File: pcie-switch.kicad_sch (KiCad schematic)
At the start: 139 parts, among them J5 Tag-Connect_TC2050-IDC-NL_2x5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, Q1 BSS138PW,115, Q2 BSS138PW,115, Q3 BSS138PW,115, Q4 BSS138PW,115, Q5 BSS138PW,115, U4 PI7C9X3G606GP, U5 NTS0302JKZ, U6 93AA66C_SOIC

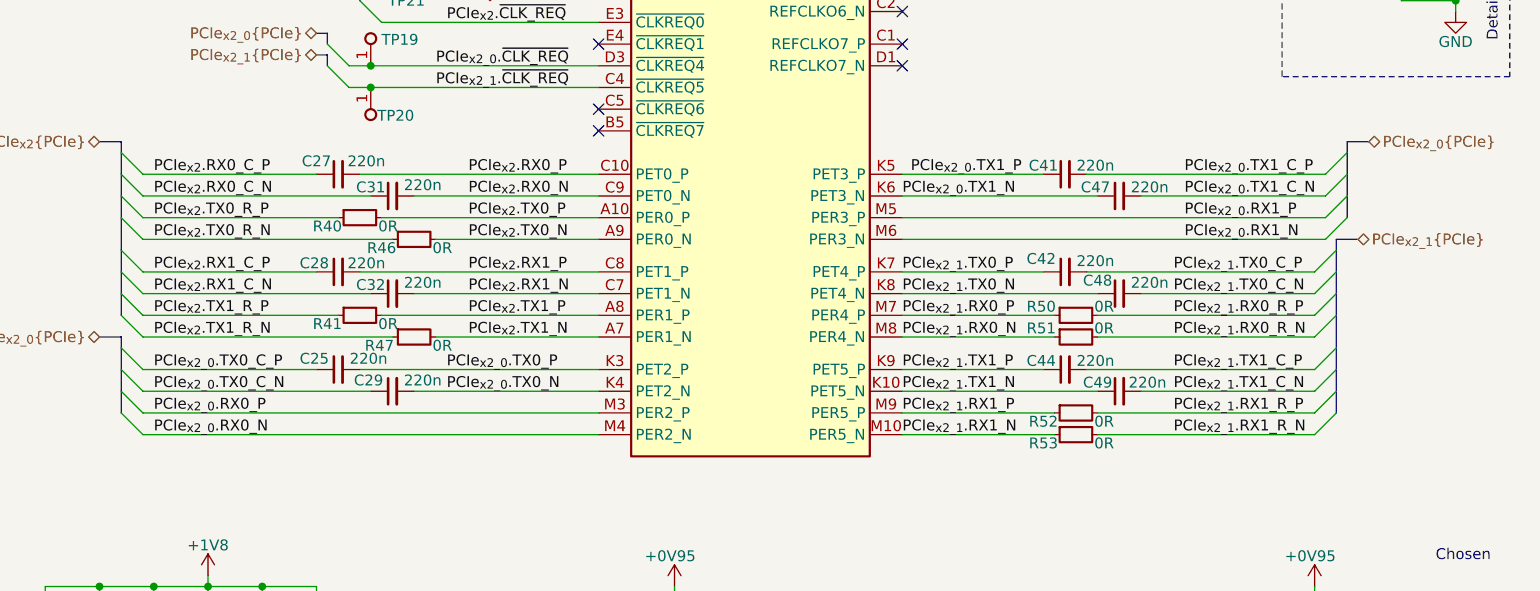
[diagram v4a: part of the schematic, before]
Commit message: [#101859] Add HS fanout from connectors
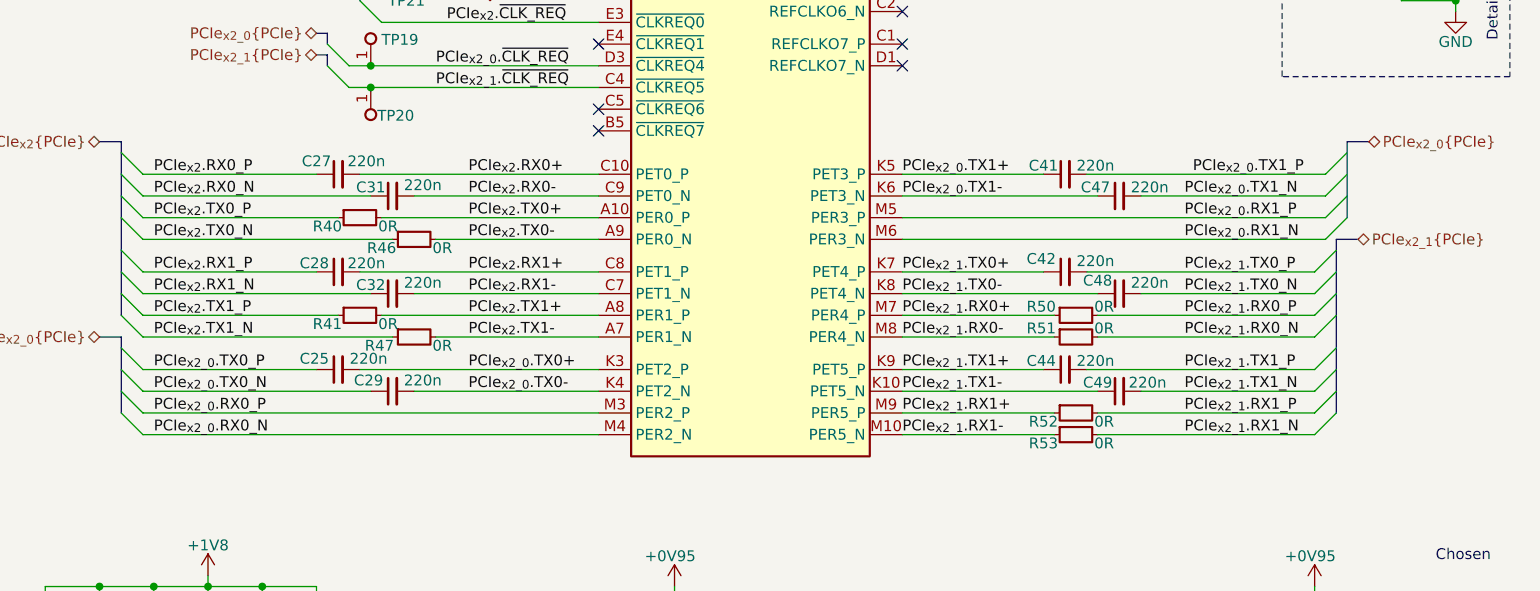
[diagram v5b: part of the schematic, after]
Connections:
- net PCIe_{x2_0}.TX0_C_N is gone; now on net PCIe_{x2_0}.TX0_N: C29.1
- net PCIe_{x2_0}.TX0_C_P is gone; now on net PCIe_{x2_0}.TX0_P: C25.1
- net PCIe_{x2_0}.TX1_C_N is gone; now on net PCIe_{x2_0}.TX1_N: C47.2
- net PCIe_{x2_0}.TX1_C_P is gone; now on net PCIe_{x2_0}.TX1_P: C41.2
- net PCIe_{x2_1}.RX0_R_N is gone; now on net PCIe_{x2_1}.RX0_N: R51.2
- net PCIe_{x2_1}.RX0_R_P is gone; now on net PCIe_{x2_1}.RX0_P: R50.2
- net PCIe_{x2_1}.RX1_R_N is gone; now on net PCIe_{x2_1}.RX1_N: R53.2
- net PCIe_{x2_1}.RX1_R_P is gone; now on net PCIe_{x2_1}.RX1_P: R52.2
- net PCIe_{x2_1}.TX0_C_N is gone; now on net PCIe_{x2_1}.TX0_N: C48.2
- net PCIe_{x2_1}.TX0_C_P is gone; now on net PCIe_{x2_1}.TX0_P: C42.2
- net PCIe_{x2_1}.TX1_C_N is gone; now on net PCIe_{x2_1}.TX1_N: C49.2
- net PCIe_{x2_1}.TX1_C_P is gone; now on net PCIe_{x2_1}.TX1_P: C44.2
- net PCIe_{x2}.RX0_C_N is gone; now on net PCIe_{x2}.RX0_N: C31.1
- net PCIe_{x2}.RX0_C_P is gone; now on net PCIe_{x2}.RX0_P: C27.1
- net PCIe_{x2}.RX1_C_N is gone; now on net PCIe_{x2}.RX1_N: C32.1
- net PCIe_{x2}.RX1_C_P is gone; now on net PCIe_{x2}.RX1_P: C28.1
- net PCIe_{x2}.TX0_R_N is gone; now on net PCIe_{x2}.TX0_N: R46.1
- net PCIe_{x2}.TX0_R_P is gone; now on net PCIe_{x2}.TX0_P: R40.1
- net PCIe_{x2}.TX1_R_N is gone; now on net PCIe_{x2}.TX1_N: R47.1
- net PCIe_{x2}.TX1_R_P is gone; now on net PCIe_{x2}.TX1_P: R41.1
- net PCIe_{x2_0}.TX0_N: no longer C29.2, U4.K4 (PET2_N)
- net PCIe_{x2_0}.TX0_P: no longer C25.2, U4.K3 (PET2_P)
- net PCIe_{x2_0}.TX1_N: no longer C47.1, U4.K6 (PET3_N)
- net PCIe_{x2_0}.TX1_P: no longer C41.1, U4.K5 (PET3_P)
- net PCIe_{x2_1}.RX0_N: no longer R51.1, U4.M8 (PER4_N)
- net PCIe_{x2_1}.RX0_P: no longer R50.1, U4.M7 (PER4_P)
- net PCIe_{x2_1}.RX1_N: no longer R53.1, U4.M10 (PER5_N)
- net PCIe_{x2_1}.RX1_P: no longer R52.1, U4.M9 (PER5_P)
- net PCIe_{x2_1}.TX0_N: no longer C48.1, U4.K8 (PET4_N)
- net PCIe_{x2_1}.TX0_P: no longer C42.1, U4.K7 (PET4_P)
- net PCIe_{x2_1}.TX1_N: no longer C49.1, U4.K10 (PET5_N)
- net PCIe_{x2_1}.TX1_P: no longer C44.1, U4.K9 (PET5_P)
- net PCIe_{x2}.RX0_N: no longer C31.2, U4.C9 (PET0_N)
- net PCIe_{x2}.RX0_P: no longer C27.2, U4.C10 (PET0_P)
- net PCIe_{x2}.RX1_N: no longer C32.2, U4.C7 (PET1_N)
- net PCIe_{x2}.RX1_P: no longer C28.2, U4.C8 (PET1_P)
- net PCIe_{x2}.TX0_N: no longer R46.2, U4.A9 (PER0_N)
- net PCIe_{x2}.TX0_P: no longer R40.2, U4.A10 (PER0_P)
- net PCIe_{x2}.TX1_N: no longer R47.2, U4.A7 (PER1_N)
- net PCIe_{x2}.TX1_P: no longer R41.2, U4.A8 (PER1_P)
- new net PCIe_{x2_0}.TX0+: C25.2, U4.K3 (PET2_P)
- new net PCIe_{x2_0}.TX0-: C29.2, U4.K4 (PET2_N)
- new net PCIe_{x2_0}.TX1+: C41.1, U4.K5 (PET3_P)
- new net PCIe_{x2_0}.TX1-: C47.1, U4.K6 (PET3_N)
- new net PCIe_{x2_1}.RX0+: R50.1, U4.M7 (PER4_P)
- new net PCIe_{x2_1}.RX0-: R51.1, U4.M8 (PER4_N)
- new net PCIe_{x2_1}.RX1+: R52.1, U4.M9 (PER5_P)
- new net PCIe_{x2_1}.RX1-: R53.1, U4.M10 (PER5_N)
- new net PCIe_{x2_1}.TX0+: C42.1, U4.K7 (PET4_P)
- new net PCIe_{x2_1}.TX0-: C48.1, U4.K8 (PET4_N)
- new net PCIe_{x2_1}.TX1+: C44.1, U4.K9 (PET5_P)
- new net PCIe_{x2_1}.TX1-: C49.1, U4.K10 (PET5_N)
- new net PCIe_{x2}.RX0+: C27.2, U4.C10 (PET0_P)
- new net PCIe_{x2}.RX0-: C31.2, U4.C9 (PET0_N)
- new net PCIe_{x2}.RX1+: C28.2, U4.C8 (PET1_P)
- new net PCIe_{x2}.RX1-: C32.2, U4.C7 (PET1_N)
- new net PCIe_{x2}.TX0+: R40.2, U4.A10 (PER0_P)
- new net PCIe_{x2}.TX0-: R46.2, U4.A9 (PER0_N)
- new net PCIe_{x2}.TX1+: R41.2, U4.A8 (PER1_P)
- new net PCIe_{x2}.TX1-: R47.2, U4.A7 (PER1_N)
